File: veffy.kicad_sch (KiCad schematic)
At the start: 97 parts, among them J1 SWD, Q1 2N7002, Q2 BFR93A, Q3 2N7002, Q4 BFR93AE6327HTSA1, SW1 SW_Push, U1 ATSAMD21G18A-A, U2 ADF4112BCPZ, U3 SA612AN/01_112, U4 MC3361, U5 LM386, U6 LM358_DFN, U7 AD9834, U8 QPA9510, Y2 TCXO-14

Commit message: TX power amp is done!
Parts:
- added C46: 22pF, symbol Device:C
- added C47: 27pF, symbol Device:C
- added C48: 2pF, symbol Device:C
- added C49: 56pF, symbol Device:C
- added J2: Conn_Coaxial, symbol Connector:Conn_Coaxial
- added L13: 1uH, symbol Device:L
- added L14: 2.7nH, symbol Device:L
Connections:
- net +3.3V: now also L13.2
- net GND: now also C46.2, C47.2, C48.2, J2.2 (Ext)
- net PA_DIE_OUT: now reaches U8.10 (RFOUT)
- net PA_DIE_OUT: now also U8.11 (RFOUT), U8.12 (RFOUT), U8.9 (RFOUT), C47.1, L13.1, L14.1
- net ANT: no longer names the net of C36.1
- net ANT: now also J2.1 (In)
- new net: C46.1, C48.1, C49.1, L14.2
- new net TX_BAND_INT: C49.2
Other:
- moved on the sheet: C40, C41, L10, L7, L8, L9, R23, R24, R25, R26, U8

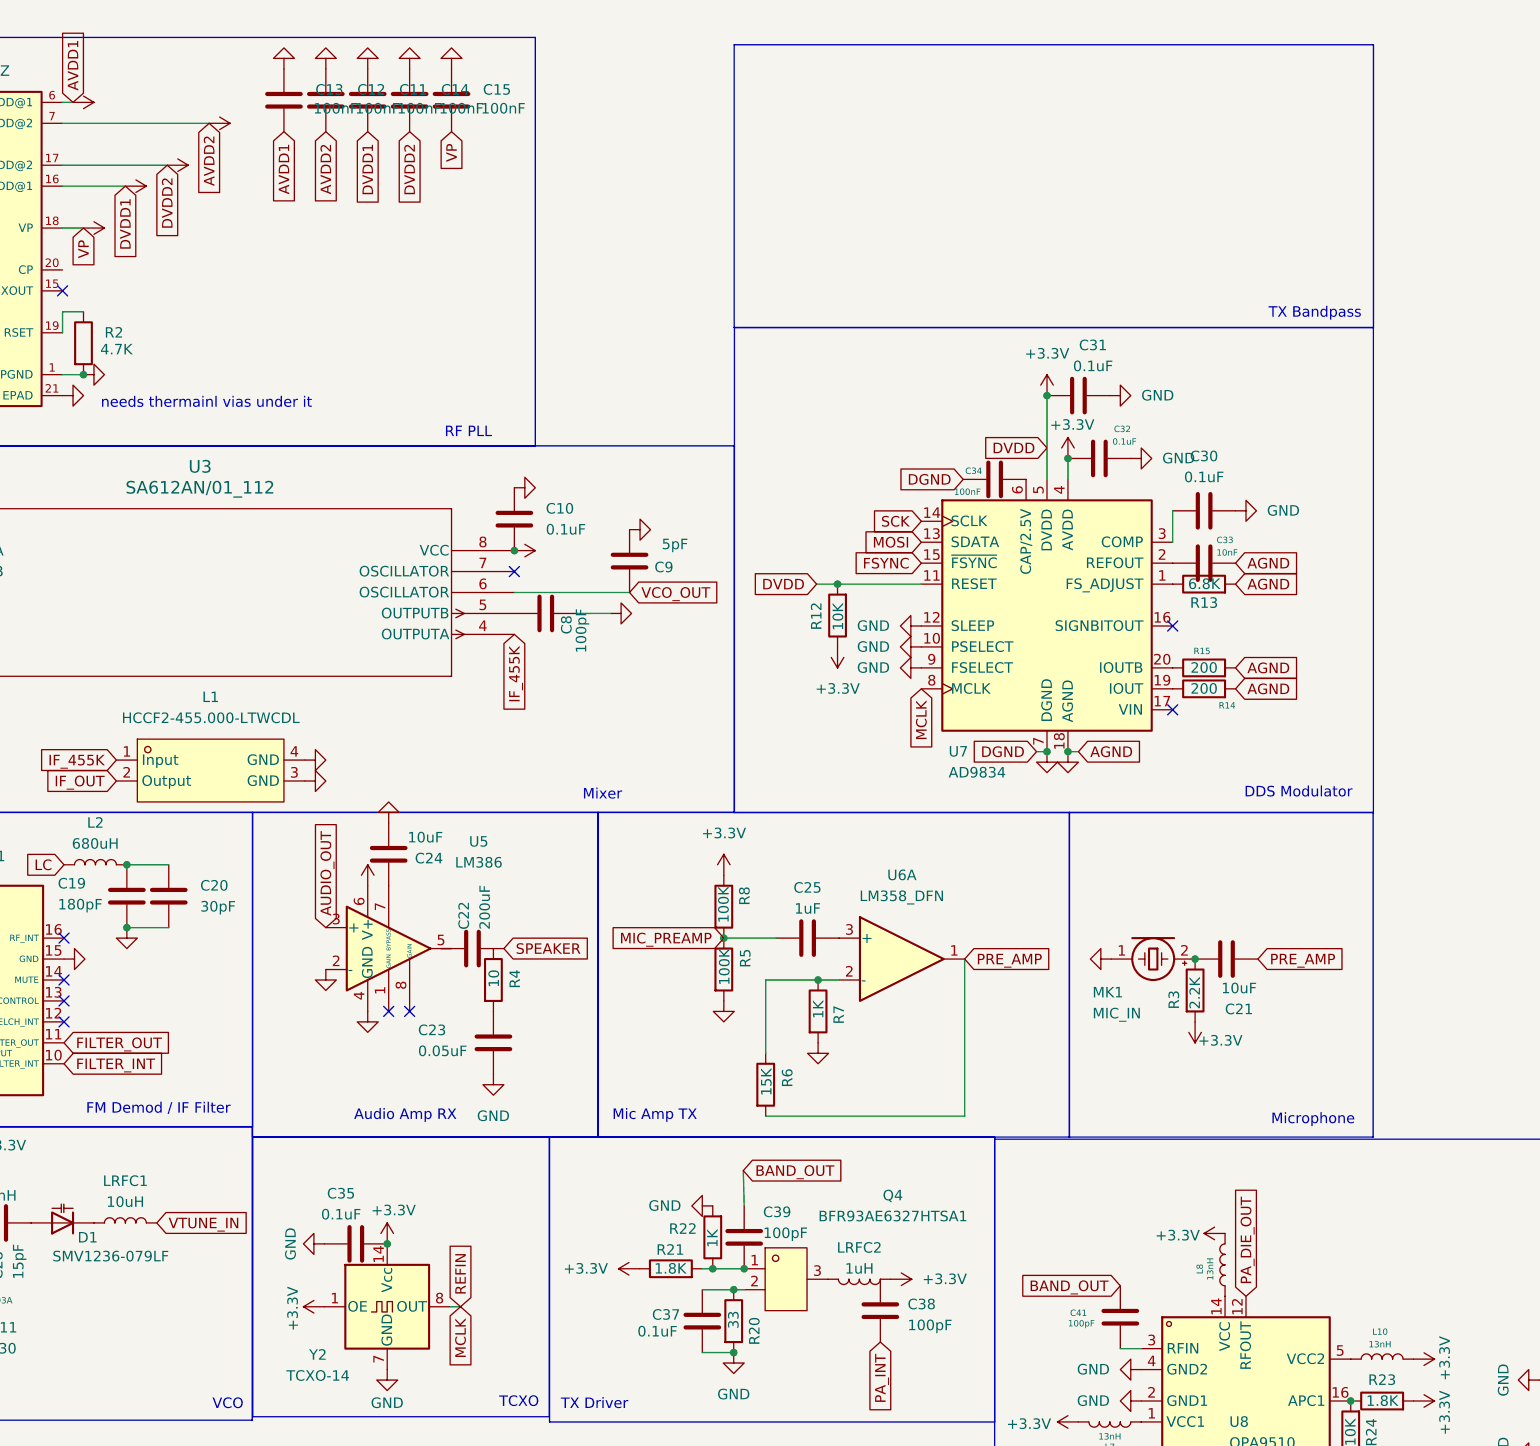
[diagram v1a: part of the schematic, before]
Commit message: made the TX Output Low-Pass Filter!
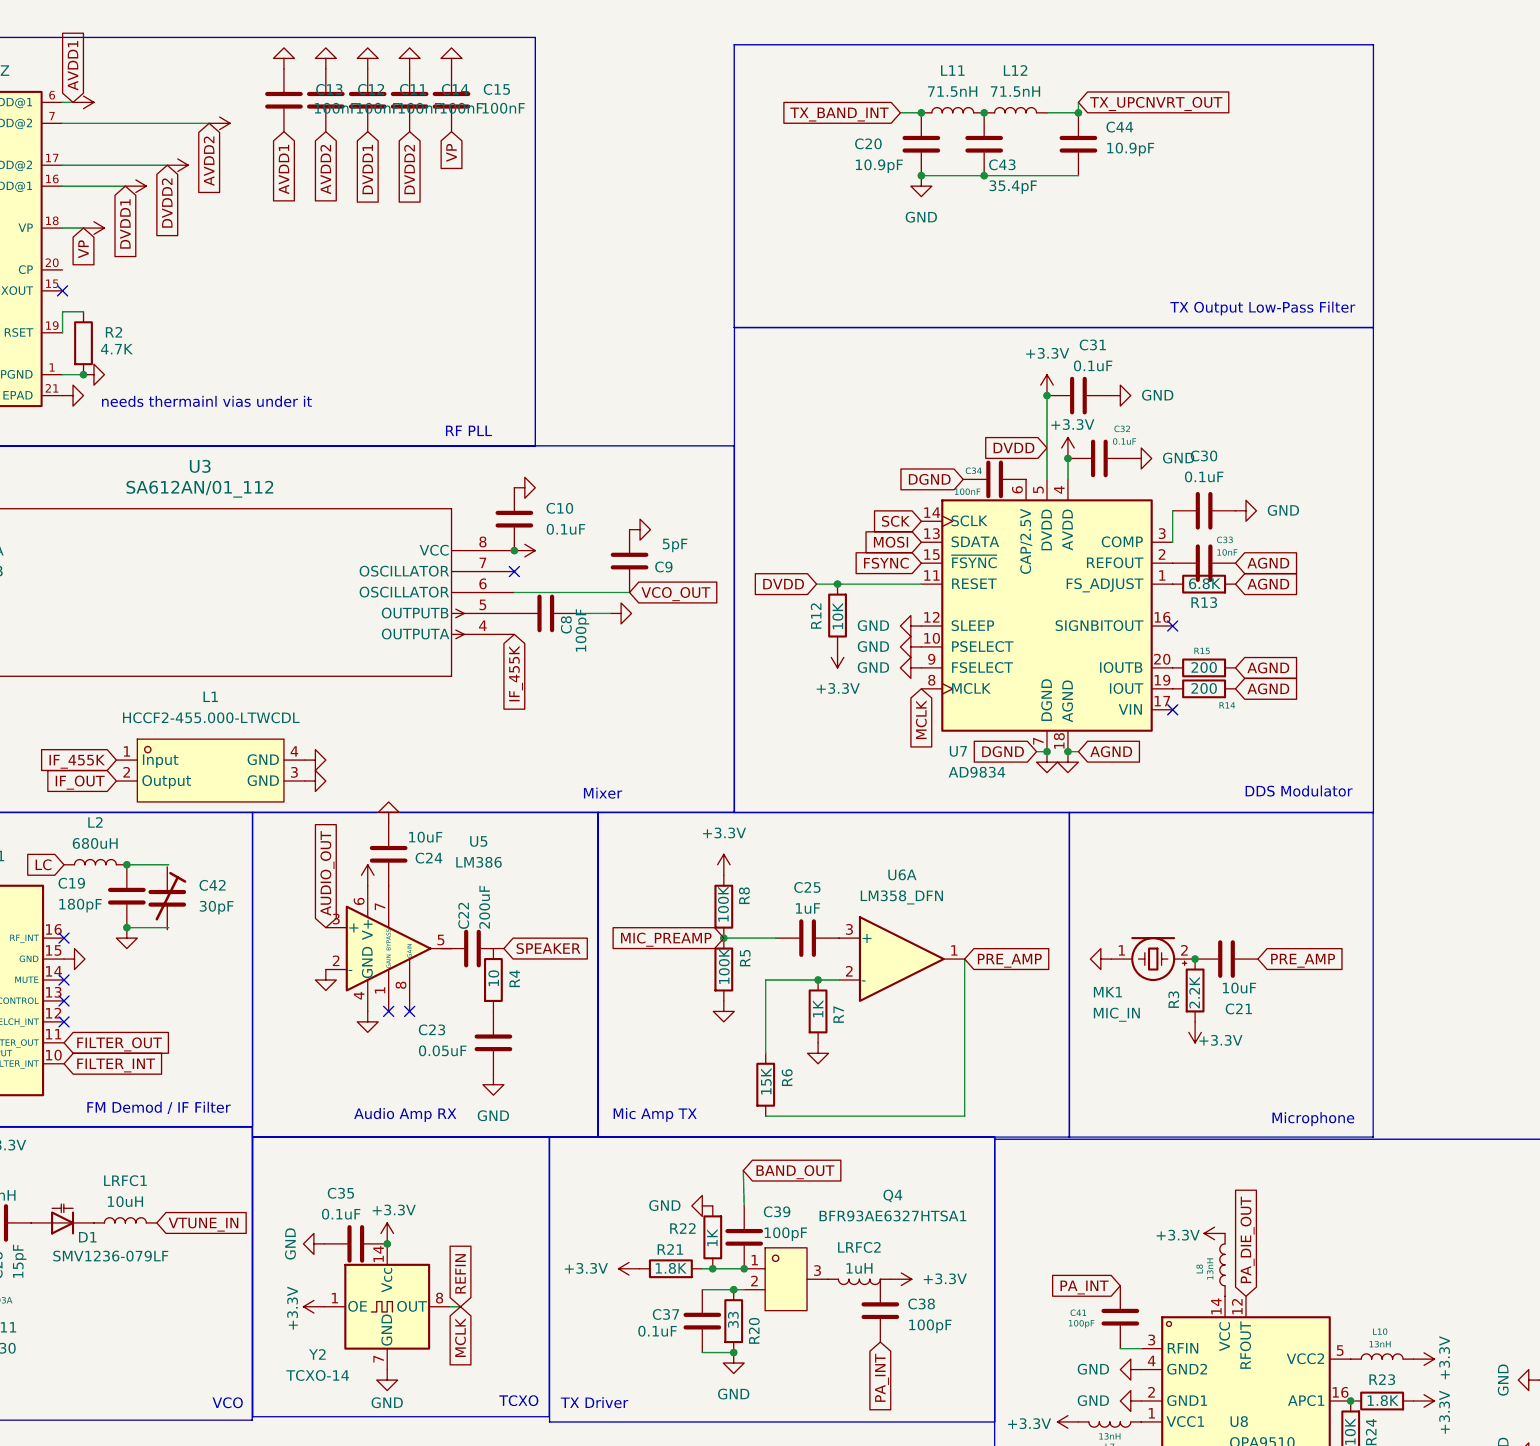
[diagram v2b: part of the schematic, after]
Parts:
- added C42: 30pF, symbol Device:C_Trim
- added C43: 35.4pF, symbol Device:C
- added C44: 10.9pF, symbol Device:C
- added L11, L12: 71.5nH, symbol Device:L
- C20: value 30pF -> 10.9pF; footprint Capacitor_SMD:C_0603_1608Metric_Pad1.08x0.95mm_HandSolder -> (none)
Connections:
- net BAND_OUT: no longer C41.1
- net GND: now also C20.1, C43.1, C44.1; no longer C20.2
- net PA_INT: now also C41.1
- net TX_BAND_INT: now also C20.2, L11.1
- net at C19.1, L2.2: no longer C20.1
- new net: C43.2, L11.2, L12.1
- new net TX_UPCNVRT_OUT: C44.2, L12.2
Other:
- note added: "TX Output Low-Pass Filter"
- note removed: "TX Bandpass"

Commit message: rx pre-selector done
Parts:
- added C45: 0.7pF, symbol Device:C
- added L15: 280nH, Inductor_SMD:L_0603_1608Metric, symbol Device:L
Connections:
- net GND: now also C45.2
- net RX_EN: now also Q1.1 (G); no longer Q1.3 (D)
- net RX_MIX_INT: now also C45.1, L15.2
- net TX_EN: now also Q3.1 (G); no longer Q3.3 (D)
- net RX_RF: now reaches D2.1
- net RX_RF: now also Q1.2 (S), L15.1; no longer Q1.1 (G)
- net at L4.2: now also Q1.3 (D); no longer Q1.2 (S)
- net at D2.2: now also Q3.2 (S); no longer Q3.1 (G)
- net at L5.2: now also Q3.3 (D); no longer Q3.2 (S)
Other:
- note added: "RX Preselector"
- moved on the sheet: L4, L5, Q1, Q3, R16, R17, R18, R19

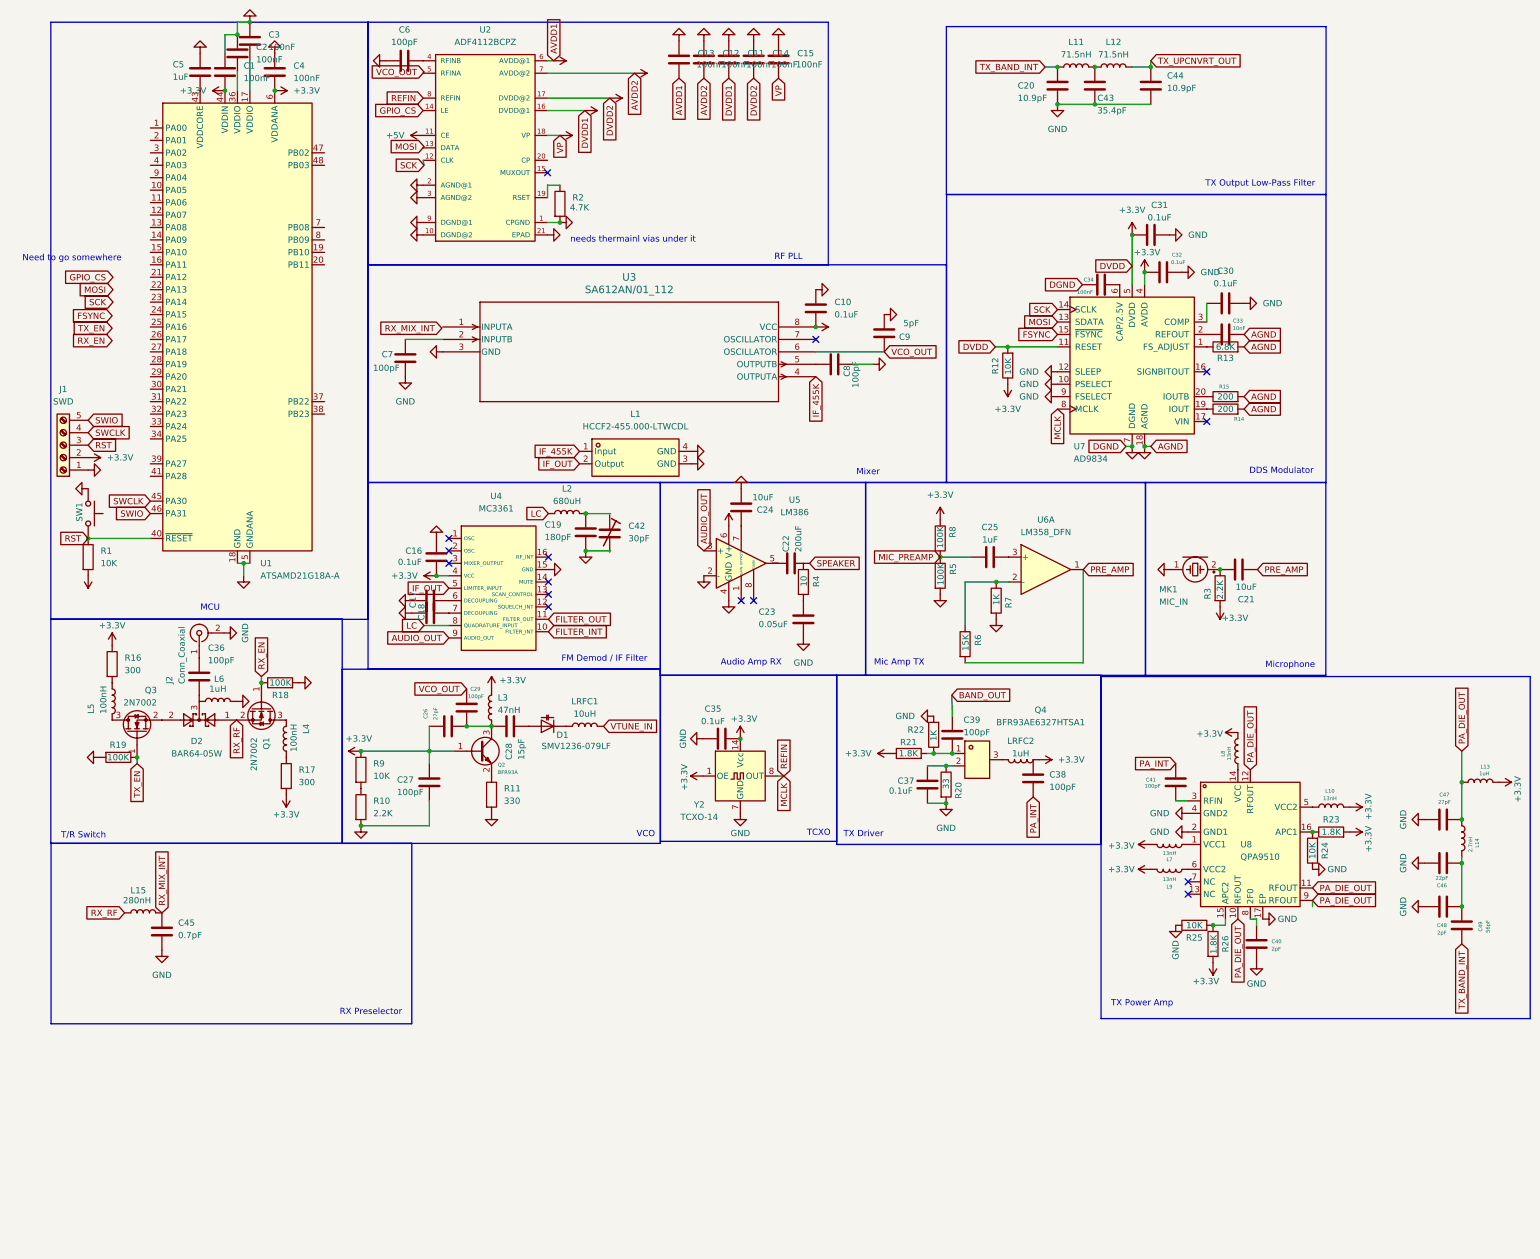
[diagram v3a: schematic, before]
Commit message: MCU GPIO done + the RX Preselector
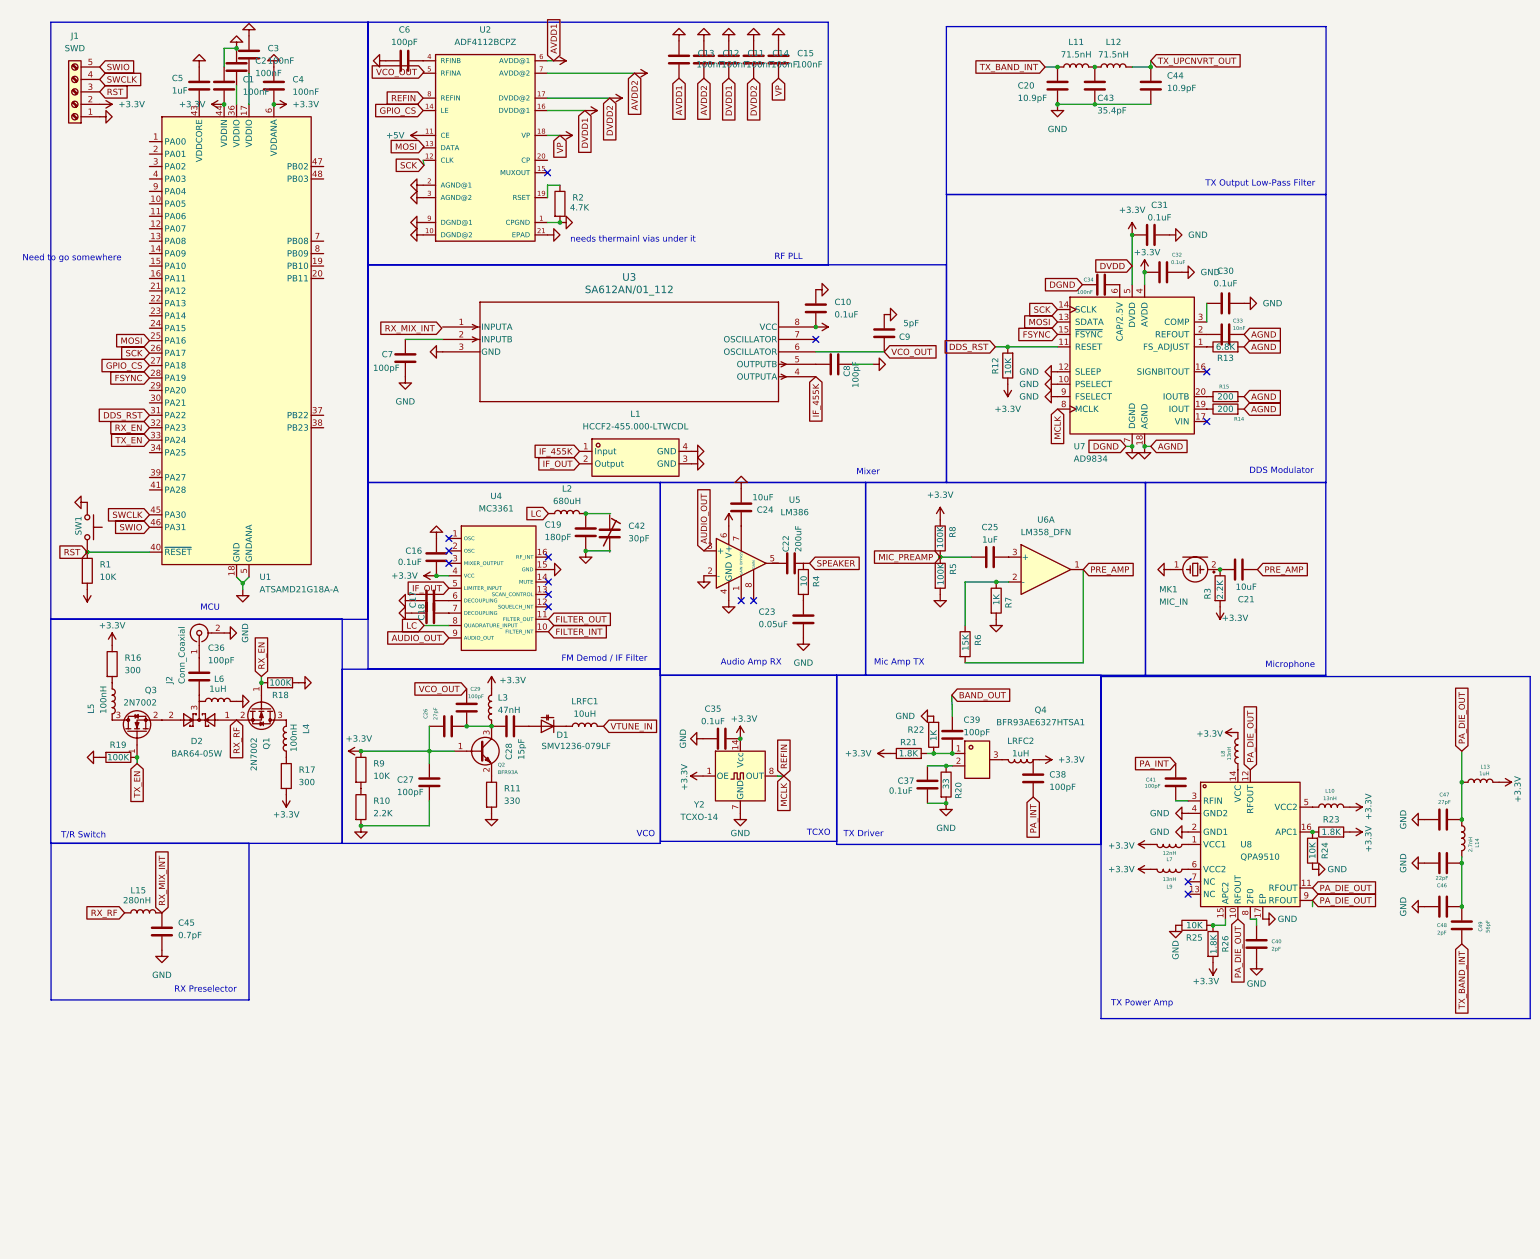
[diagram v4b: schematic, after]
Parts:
- L7: value 13nH -> 12nH
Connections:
- net +3.3V: no longer R12.2, U7.11 (RESET)
- net FSYNC: now also U1.28 (PA19)
- net GPIO_CS: now also U1.27 (PA18)
- net MOSI: now also U1.25 (PA16)
- net RX_EN: now also U1.32 (PA23)
- net SCK: now also U1.26 (PA17)
- net TX_EN: now also U1.33 (PA24)
- net DDS_RST: now reaches U1.31 (PA22)
- net DDS_RST: now also R12.2, U7.11 (RESET)
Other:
- moved on the sheet: C1, C2, C3, C4, C5, J1, R1, SW1, U1

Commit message: usb c done
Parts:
- removed L15: 280nH, Inductor_SMD:L_0603_1608Metric, symbol Device:L
- added C50: 0.7pF, Capacitor_SMD:C_0603_1608Metric_Pad1.08x0.95mm_HandSolder, symbol Device:C
- added CN1: XH-2AW_C2908611, LCSC:CONN-TH_XH-2AW_C2908611, symbol Easyeda2Kicad:XH-2AW_C2908611
- added FB1: FerriteBead, symbol Device:FerriteBead
- added J3: USB_C_Receptacle_USB2.0_14P, Connector_USB:USB_C_Receptacle_HRO_TYPE-C-31-M-17, symbol Connector:USB_C_Receptacle_USB2.0_14P
- added L16: 280nH, Inductor_SMD:L_0603_1608Metric, symbol Device:L
- added R27, R28: 5.1K, Resistor_SMD:R_0603_1608Metric_Pad0.98x0.95mm_HandSolder, symbol Device:R
- C20, C43, C44, C46, C47, C48, C49: footprint (none) -> Capacitor_SMD:C_0603_1608Metric_Pad1.08x0.95mm_HandSolder
- C36, C37, C38, C39, C40, C41: footprint Capacitor_SMD:C_0603_1608Metric -> Capacitor_SMD:C_0603_1608Metric_Pad1.08x0.95mm_HandSolder
- C45: value 0.7pF -> C; footprint (none) -> Capacitor_SMD:C_0603_1608Metric_Pad1.08x0.95mm_HandSolder
- L1: footprint easyeda2kicad:FILTER-SMD_4P-L11.9-W6.5-P5.50-LS7.5-BL -> LCSC:FILTER-SMD_4P-L11.9-W6.5-P5.50-LS7.5-BL
- L11, L12, L13, L14, LRFC1, LRFC2: footprint (none) -> Inductor_SMD:L_0603_1608Metric
- R23, R24, R25, R26: footprint (none) -> Resistor_SMD:R_0603_1608Metric_Pad0.98x0.95mm_HandSolder
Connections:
- net +5V: now also R27.2, R28.1
- net GND: now also C45.1, C50.2, FB1.1; no longer C45.2
- net RX_MIX_INT: now also C50.1, L16.2; no longer C45.1
- net RX_RF: now also L16.1
- net TX_EN: now also U1.22 (PA13); no longer U1.33 (PA24)
- net D+: now reaches U1.34 (PA25)
- net D+: now also J3.A6 (D+), J3.B6 (D+)
- new net: FB1.2, J3.A1 (GND), J3.A12 (GND), J3.B1 (GND), J3.B12 (GND), J3.SH (SHIELD)
- new net: J3.A5 (CC1), R28.2
- new net: J3.B5 (CC2), R27.1
- new net D-: J3.A7 (D-), J3.B7 (D-), U1.33 (PA24)
- new net VBUS: C45.2, J3.A4 (VBUS), J3.A9 (VBUS), J3.B4 (VBUS), J3.B9 (VBUS)
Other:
- note added: "USB-C Flashing"

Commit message: battery charging circuit is done!
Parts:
- added C51, C52: 4.7uF, symbol Device:C
- added R29: 2K, symbol Device:R
- added U9: MCP73831-2-OT, Package_TO_SOT_SMD:SOT-23-5, symbol Battery_Management:MCP73831-2-OT
- C45: value C -> 0.1uF
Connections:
- net +5V: no longer R27.2, R28.1
- net GND: now also CN1.2, R27.2, R28.1, C51.1, C52.1, R29.1, U9.2 (V_{SS})
- net VBUS: now also C51.2, U9.4 (V_{DD})
- net BAT+: now reaches CN1.1
- net BAT+: now also C52.2, U9.3 (V_{BAT})
- new net: R29.2, U9.5 (PROG)
- no-connect marks 15 -> 16
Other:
- note added: "Battery Charging"
- moved on the sheet: CN1
